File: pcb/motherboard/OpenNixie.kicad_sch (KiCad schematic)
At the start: 48 parts, among them J1 Conn_01x02, J10 Nixie_Conn_12P, J11 Nixie_Conn_12P, J2 Conn_01x02, J3 Conn_01x03, J4 Nixie_Conn_4P, J5 Conn_01x04, J6 12V, J7 Conn_01x03, J8 Nixie_Conn_12P, J9 Nixie_Conn_12P, Q1 MPSA42, Q2 MPSA42, Q3 TK8P65W, U1 LM7805_TO220, U2 NE555P, U3 NE555P, U4 MAX1771CSA, U5 DS3231M, U6 74LS138, U7 74HC595, U8 74LS138

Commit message: Ver 3.0
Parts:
- removed BT1: 3V, Connector_JST:JST_EH_B2B-EH-A_1x02_P2.50mm_Vertical, symbol Device:Battery_Cell
- removed J1: Conn_01x02, Connector_JST:JST_EH_B2B-EH-A_1x02_P2.50mm_Vertical, symbol Connector_Generic:Conn_01x02
- removed Q2: MPSA42, Package_TO_SOT_THT:TO-92_Inline, symbol Transistor_BJT:MPSA42
- removed R10, R9: 10k, Resistor_THT:R_Axial_DIN0204_L3.6mm_D1.6mm_P2.54mm_Vertical, symbol Device:R_Small
- removed U5: DS3231M, Package_SO:SOIC-16W_7.5x10.3mm_P1.27mm, symbol Timer_RTC:DS3231M
- added Q2: S8050, Package_TO_SOT_THT:TO-92_Inline, symbol Transistor_BJT:S8050
- R1: value 150k -> 47k; footprint Resistor_THT:R_Axial_DIN0204_L3.6mm_D1.6mm_P2.54mm_Vertical -> Resistor_THT:R_Axial_DIN0204_L3.6mm_D1.6mm_P5.08mm_Horizontal
- R10: renamed from R12; value 10k -> 6.8k; footprint Resistor_THT:R_Axial_DIN0204_L3.6mm_D1.6mm_P2.54mm_Vertical -> Resistor_THT:R_Axial_DIN0309_L9.0mm_D3.2mm_P12.70mm_Horizontal
- R11: renamed from R13; footprint Resistor_THT:R_Axial_DIN0204_L3.6mm_D1.6mm_P2.54mm_Vertical -> Resistor_THT:R_Axial_DIN0204_L3.6mm_D1.6mm_P5.08mm_Horizontal
- R12: renamed from R15; footprint Resistor_THT:R_Axial_DIN0204_L3.6mm_D1.6mm_P2.54mm_Vertical -> Resistor_THT:R_Axial_DIN0204_L3.6mm_D1.6mm_P5.08mm_Horizontal
- R2, R4, R5, R6, R7, R8: footprint Resistor_THT:R_Axial_DIN0204_L3.6mm_D1.6mm_P2.54mm_Vertical -> Resistor_THT:R_Axial_DIN0204_L3.6mm_D1.6mm_P5.08mm_Horizontal
- R3: value 150k -> 470k; footprint Resistor_THT:R_Axial_DIN0204_L3.6mm_D1.6mm_P2.54mm_Vertical -> Resistor_THT:R_Axial_DIN0204_L3.6mm_D1.6mm_P5.08mm_Horizontal
- R9: renamed from R11; footprint Resistor_THT:R_Axial_DIN0204_L3.6mm_D1.6mm_P2.54mm_Vertical -> Resistor_THT:R_Axial_DIN0204_L3.6mm_D1.6mm_P5.08mm_Horizontal
- renumbered J2 to J1, J11 to J10, J3 to J2, J4 to J3, J5 to J4, J7 to J5, J8 to J7, J9 to J8, J10 to J9, R14 to R13, U6 to U5, U7 to U6, U8 to U7
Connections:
- net +12V: now also J4.3 (Pin_3), R2.2, U2.4 (R), U2.8 (VCC); no longer J4.2 (Pin_2)
- net +170V: now also J4.2 (Pin_2), R10.1; no longer J4.3 (Pin_3), R10.2
- net +5V: now also R6.1; no longer R2.2, R6.2, U2.4 (R), U2.8 (VCC)
- net GND: now also C5.2, R11.2, R9.1, Q2.1 (E); no longer C5.1, R11.1, R9.2
- net LIGHT_PIN: now also R6.2; no longer R6.1
- net SHDN_PIN: now also R9.2; no longer R9.1
- net SR_CLK: now also J2.1 (Pin_1); no longer J2.3 (Pin_3)
- net SR_LATCH: now also J2.3 (Pin_3); no longer J2.1 (Pin_1)
- net at U3.3 (Q): now also R5.2; no longer R5.1
- net at U4.5 (REF): now also C5.1; no longer C5.2
- net at C4.1, D2.1 (K): now also R10.2, R8.2; no longer R10.1, R8.1
- net at D1.2 (A), R1.1: now also Q2.3 (C)
- net NPN_X_P0 renamed NOT_X_P0
- net NPN_X_P1 renamed NOT_X_P1
- net NPN_X_P2 renamed NOT_X_P2
- net NPN_X_P3 renamed NOT_X_P3
- new net: R11.1, R8.1, U4.3 (FB)
- new net: Q2.2 (B), R5.1
- no-connect marks 18 -> 15
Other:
- note added: "Use capacitor with withstanding voltage more than 450V."
- note removed: "DS3231 RTC Module"
- note removed: "Use capacitor with withstanding voltage more than 300V."
- moved on the sheet: C2, C3, C4, C5, D2, D3, J10, J2, J5, J7, J8, J9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

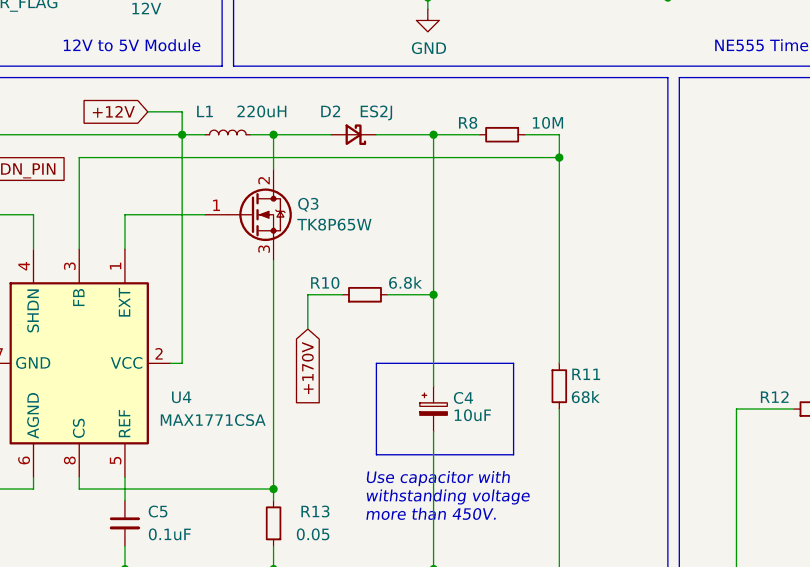
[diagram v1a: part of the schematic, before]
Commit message: Update resistor value
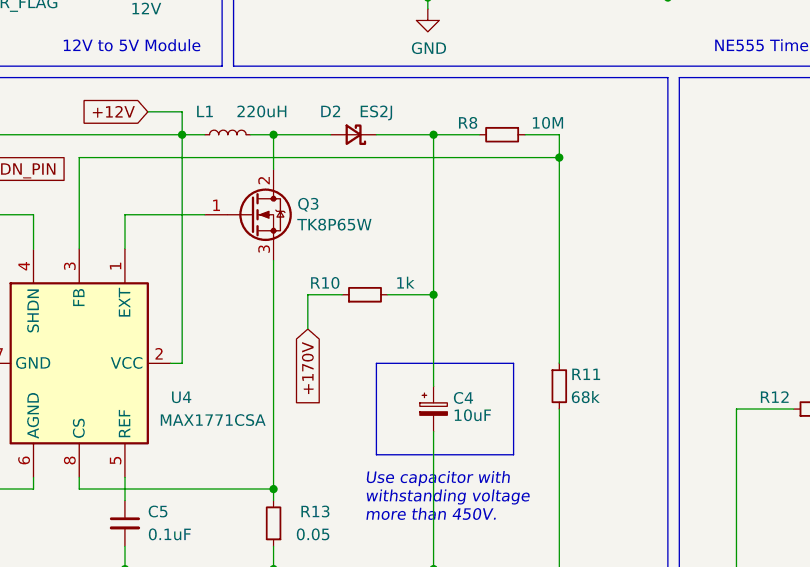
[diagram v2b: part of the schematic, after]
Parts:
- R10: value 6.8k -> 1k
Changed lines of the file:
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@@
       (effects (font (size 1.27 1.27)))
     )
-    (property "Value" "6.8k" (at 83.82 77.47 90)
+    (property "Value" "1k" (at 83.82 77.47 90)
       (effects (font (size 1.27 1.27)))
     )

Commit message: PCB updated
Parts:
- removed C1: 470uF, Capacitor_THT:CP_Radial_D8.0mm_P3.50mm, symbol Device:C_Polarized_Small
- removed C2: 10uF, Capacitor_THT:CP_Radial_D5.0mm_P2.00mm, symbol Device:C_Polarized_Small
- removed D1: 1N4148, Diode_THT:D_DO-35_SOD27_P2.54mm_Vertical_AnodeUp, symbol Diode:1N4148
- removed D3: LED_RKGB, LED_THT:LED_D5.0mm-4_RGB_Wide_Pins, symbol Device:LED_RKGB
- removed J1: Conn_01x02, Connector_JST:JST_EH_B2B-EH-A_1x02_P2.50mm_Vertical, symbol Connector_Generic:Conn_01x02
- removed J2, J5: Conn_01x03, Connector_JST:JST_EH_B3B-EH-A_1x03_P2.50mm_Vertical, symbol Connector_Generic:Conn_01x03
- removed J3: Nixie_Conn_4P, Nixie_Clock:Nixie_Conn_4P, symbol Nixie_Clock:Nixie_Conn_4P
- removed J4: Conn_01x04, Connector_JST:JST_EH_B4B-EH-A_1x04_P2.50mm_Vertical, symbol Connector_Generic:Conn_01x04
- removed J6: 12V, Connector_BarrelJack:BarrelJack_Horizontal, symbol Connector:Barrel_Jack_Switch_Pin3Ring
- removed Q1: MPSA42, Package_TO_SOT_THT:TO-92_Inline, symbol Transistor_BJT:MPSA42
- removed Q2: S8050, Package_TO_SOT_THT:TO-92_Inline, symbol Transistor_BJT:S8050
- removed R10: 1k, Resistor_THT:R_Axial_DIN0309_L9.0mm_D3.2mm_P12.70mm_Horizontal, symbol Device:R_Small
- removed R12: 1k, Resistor_THT:R_Axial_DIN0204_L3.6mm_D1.6mm_P5.08mm_Horizontal, symbol Device:R_Small
- removed R3: 470k, Resistor_THT:R_Axial_DIN0204_L3.6mm_D1.6mm_P5.08mm_Horizontal, symbol Device:R_Small
- removed R4, R5: 10k, Resistor_THT:R_Axial_DIN0204_L3.6mm_D1.6mm_P5.08mm_Horizontal, symbol Device:R_Small
- removed R6, R7: 150k, Resistor_THT:R_Axial_DIN0204_L3.6mm_D1.6mm_P5.08mm_Horizontal, symbol Device:R_Small
- removed RV1: 200k, Potentiometer_THT:Potentiometer_Vishay_T73YP_Vertical, symbol Device:R_Potentiometer_Small
- removed U1: LM7805_TO220, Package_TO_SOT_THT:TO-220-3_Vertical, symbol Regulator_Linear:LM7805_TO220
- removed U2, U3: NE555P, Package_DIP:DIP-8_W7.62mm, symbol Timer:NE555P
- removed U5, U7: 74LS138, Package_DIP:DIP-16_W7.62mm, symbol 74xx:74LS138
- added C1: 0.1uF, Capacitor_THT:C_Disc_D3.0mm_W2.0mm_P2.50mm, symbol Device:C_Small
- added H1, H2, H3, H4: MountingHole, MountingHole:MountingHole_3.2mm_M3, symbol Mechanical:MountingHole
- added J1: Jack-DC, Connector_BarrelJack:BarrelJack_Horizontal, symbol Connector:Jack-DC
- added J6: Conn_01x05, Connector_PinHeader_2.54mm:PinHeader_1x05_P2.54mm_Vertical, symbol Connector_Generic:Conn_01x05
- added NE1: Lamp_Neon, Connector_PinSocket_2.54mm:PinSocket_1x02_P2.54mm_Vertical, symbol Device:Lamp_Neon
- added Q1: MPSA42, Package_TO_SOT_THT:TO-92_Inline, symbol PCM_Transistor_BJT_AKL:MPSA42
- added U1: AMS1117, Package_TO_SOT_SMD:SOT-223-3_TabPin2, symbol Regulator_Linear:AMS1117
- added U4: 74HC595, Package_DIP:DIP-16_W7.62mm, symbol 74xx:74HC595
- R1: value 47k -> 10M
- R2: value 1k -> 47k
- R4: renamed from R9; value 10k -> 47k
- renumbered C3 to C2, C4 to C3, C5 to C4, D2 to D1, J7 to J2, J8 to J3, J9 to J4, J10 to J5, Q3 to Q2, R8 to R3, R11 to R5, R13 to R6, U4 to U2, U6 to U3
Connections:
- net GND: now also R4.2, C1.2, J1.2, J6.5 (Pin_5), Q1.1 (E), U1.1 (ADJ), U4.13 (~{OE}), U4.8 (GND); no longer R4.1
- net SR_DATA: now also J6.2 (Pin_2)
- net SR_LATCH: now also J6.1 (Pin_1), U4.12 (RCLK)
- net +170v: now reaches C3.1, D1.1 (K), R3.2
- net +170v: now also NE1.1
- net at R1.1: now also Q1.3 (C)
- net SR_CASCADE: now reaches U3.9 (QH')
- net SR_CASCADE: now also U4.14 (SER)
- net SYMBOL: now reaches R2.1
- net SYMBOL: now also U4.6 (QG)
- net +12V renamed +12v
- net +12v: now also J1.1, U1.3 (VI); no longer R2.2
- net +5V renamed +5v
- net +5v: now also C1.1, J6.4 (Pin_4), U1.2 (VO), U4.10 (~{SRCLR}), U4.16 (VCC); no longer R1.2
- net DECODER_P0 renamed SR_SEG_P0
- net DECODER_P1 renamed SR_SEG_P1
- net DECODER_P2 renamed SR_SEG_P2
- net DECODER_P3 renamed SR_SEG_P3
- net NIXIE_X_P0 renamed BIT_P0
- net NIXIE_X_P1 renamed BIT_P1
- net NIXIE_X_P2 renamed BIT_P2
- net NIXIE_X_P3 renamed BIT_P3
- net NIXIE_Y_P0 renamed SEG_P0
- net NIXIE_Y_P1 renamed SEG_P1
- net NIXIE_Y_P2 renamed SEG_P2
- net NIXIE_Y_P3 renamed SEG_P3
- net NIXIE_Y_P4 renamed SEG_P4
- net NIXIE_Y_P5 renamed SEG_P5
- net NIXIE_Y_P6 renamed SEG_P6
- net NIXIE_Y_P7 renamed SEG_P7
- net NIXIE_Y_P8 renamed SEG_P8
- net NIXIE_Y_P9 renamed SEG_P9
- net NOT_X_P0 renamed SR_SEG_P4
- net NOT_X_P1 renamed SR_SEG_P5
- net NOT_X_P2 renamed SR_SEG_P6
- net NOT_X_P3 renamed SR_SEG_P7
- net SHDN_PIN renamed ENABLE
- net ENABLE: now also R4.1, U4.7 (QH); no longer R4.2
- net SR_CLK renamed SR_CLOCK
- net SR_CLOCK: now also J6.3 (Pin_3), U4.11 (SRCLK)
- new net: Q1.2 (B), R2.2
- new net: NE1.2, R1.2
- new net SR_BIT_P0: U4.2 (QC)
- new net SR_BIT_P1: U4.3 (QD)
- new net SR_BIT_P2: U4.4 (QE)
- new net SR_BIT_P3: U4.5 (QF)
- new net SR_SEG_P8: U4.15 (QA)
- new net SR_SEG_P9: U4.1 (QB)
- no-connect marks 15 -> 5
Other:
- removed sheet Decoder Inverter
- removed sheet Nixie X-axes
- removed sheet Nixie Y-axes
- added sheet Bit Select (NixieBS.kicad_sch)
- added sheet Segment Select (NixieSS.kicad_sch)
- note added: "Use capacitor with withstanding voltage more than 200V."
- note removed: "12V to 170V Boost Converter Module"
- note removed: "12V to 5V Module"
- note removed: "NE555 Timer Module"
- note removed: "Neon Lamp Blinking Module"
- note removed: "Nixie Controller Module"
- note removed: "Nixie Decoding Module"
- note removed: "Nixie Socket Module"
- note removed: "Power & Peripherals Interface Module"
- note removed: "RGB Module"
- note removed: "Use capacitor with withstanding voltage more than 450V."
- moved on the sheet: C2, C3, C4, D1, J2, J3, J4, J5, L1, Q2, R3, R4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

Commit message: Some fixes
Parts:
- R1: value 10M -> 1M
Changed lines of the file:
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@@
       (effects (font (size 1.27 1.27)))
     )
-    (property "Value" "10M" (at 130.81 21.59 90)
+    (property "Value" "1M" (at 130.81 21.59 90)
       (effects (font (size 1.27 1.27)))
     )
